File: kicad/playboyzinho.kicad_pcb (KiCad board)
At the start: 2 copper layers, 143.2 x 185.5 mm, 16 parts, among them SW1 SW_Push, SW2 SW_Push, SW3 SW_Push, SW4 SW_Push, SW5 SW_Push, SW6 SW_Push, SW7 SW_Push, SW8 SW_Push, SW9 SW_SPDT, U1 esp32-s3-pl, U7 (amplificador)_MAX98357_Module

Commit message: fix: corrige 90 graus
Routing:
- net /Button-2: track 93.2 -> 79.3 mm
- net /Button-3: track 106.6 -> 93.1 mm
- net /Button-4: track 86.4 -> 81.2 mm
- net /Button-1: track 88.0 -> 84.5 mm
- net /Button-5: track 52.0 -> 49.0 mm
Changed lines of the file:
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@@
+	)
+	(segment
+		(start 9.9385 84.4)
+		(end 18.0385 92.5)
+		(width 0.3)
+		(layer "F.Cu")
+		(net "/Button-4")
+	)
+	(segment
+		(start 21.87 94.5)
+		(end 21.87 123)
+		(width 0.3)
+		(layer "F.Cu")
+		(net "/Button-4")
 	)
 	(segment
@@
 	)
 	(segment
-		(start 28.87 92.5)
-		(end 28.87 130)
-		(width 0.3)
-		(layer "F.Cu")
-		(net "/Button-4")
-	)
-	(segment
-		(start 9.9385 84.4)
-		(end 18.0385 92.5)
-		(width 0.3)
-		(layer "F.Cu")
-		(net "/Button-4")
-	)
-	(segment
-		(start 28.87 130)
+		(start 18.0385 92.5)
+		(end 19.87 92.5)
+		(width 0.3)
+		(layer "F.Cu")
+		(net "/Button-4")
+	)
+	(segment
+		(start 21.87 123)
 		(end 38.87 140)
 		(width 0.3)
@@
 	)
 	(segment
-		(start 18.0385 92.5)
-		(end 28.87 92.5)
+		(start 19.87 92.5)
+		(end 21.87 94.5)
 		(width 0.3)
 		(layer "F.Cu")
@@
 	)
 	(segment
-		(start 77.37 93.05)
+		(start 71.32 87)
 		(end 85.25 100.93)
 		(width 0.3)
@@
 	(segment
 		(start 22.6985 87)
-		(end 77.37 87)
+		(end 71.32 87)
 		(width 0.3)
 		(layer "F.Cu")
@@
 	)
 	(segment
-		(start 77.37 87)
-		(end 77.37 93.05)
-		(width 0.3)
-		(layer "F.Cu")
-		(net "/Button-1")
-	)
-	(segment
 		(start 20.0985 84.4)
 		(end 22.6985 87)
@@
 	)
 	(segment
-		(start 21.6585 88.5)
-		(end 68.87 88.5)
-		(width 0.3)
-		(layer "F.Cu")
-		(net "/Button-2")
-	)
-	(segment
 		(start 17.5585 84.4)
 		(end 21.6585 88.5)
@@
 	)
 	(segment
-		(start 68.87 88.5)
-		(end 68.87 112.22)
+		(start 21.6585 88.5)
+		(end 45.15 88.5)
 		(width 0.3)
 		(layer "F.Cu")
@@
 	)
 	(segment
-		(start 68.87 112.22)
+		(start 45.15 88.5)
 		(end 71.65 115)
 		(width 0.3)
@@
 	)
 	(segment
-		(start 56.37 139)
+		(start 57.37 114)
 		(end 57.37 140)
+		(width 0.3)
+		(layer "F.Cu")
+		(net "/Button-3")
+	)
+	(segment
+		(start 20.6185 90)
+		(end 33.37 90)
 		(width 0.3)
 		(layer "F.Cu")
@@
 	)
 	(segment
-		(start 56.37 90)
-		(end 56.37 139)
-		(width 0.3)
-		(layer "F.Cu")
-		(net "/Button-3")
-	)
-	(segment
-		(start 20.6185 90)
-		(end 56.37 90)
+		(start 33.37 90)
+		(end 57.37 114)
 		(width 0.3)
 		(layer "F.Cu")
@@
 	)
 	(segment
-		(start 31.87 91.5)
-		(end 32.7 92.33)
+		(start 32.7 97.33)
+		(end 32.7 108.3)
 		(width 0.3)
 		(layer "F.Cu")
@@
 	)
 	(segment
-		(start 32.7 92.33)
-		(end 32.7 108.3)
+		(start 32.7 108.3)
+		(end 32.7 120.8)
+		(width 0.3)
+		(layer "F.Cu")
+		(net "/Button-5")
+	)
+	(segment
+		(start 19.5785 91.5)
+		(end 26.87 91.5)
 		(width 0.3)
 		(layer "F.Cu")
@@
 	)
 	(segment
-		(start 19.5785 91.5)
-		(end 31.87 91.5)
-		(width 0.3)
-		(layer "F.Cu")
-		(net "/Button-5")
-	)
-	(segment
-		(start 32.7 108.3)
-		(end 32.7 120.8)
-		(width 0.3)
-		(layer "F.Cu")
+		(start 26.87 91.5)
+		(end 32.7 97.33)
+		(width 0.3)
+		(layer "F.Cu")

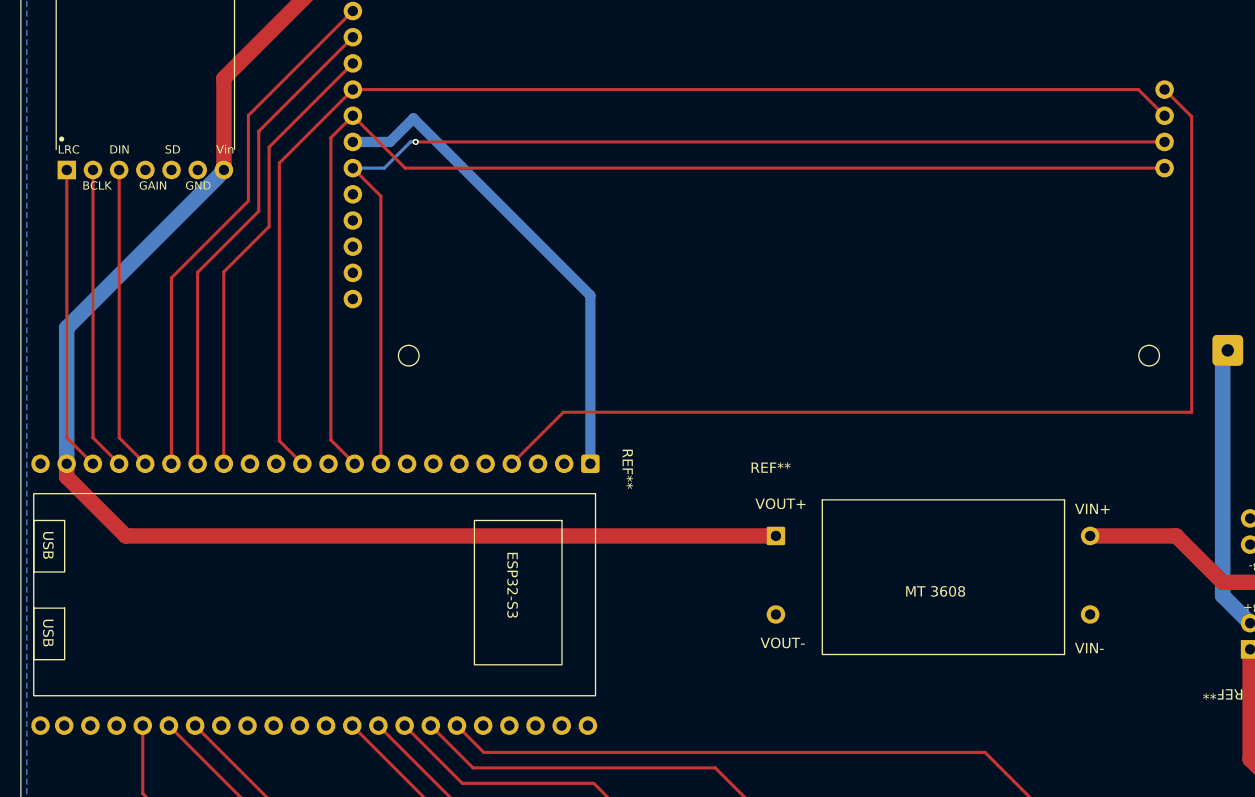
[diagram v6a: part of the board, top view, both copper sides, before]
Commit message: refact: separa conexões SD da tela e adiciona uma conexão ao SD do amplificador
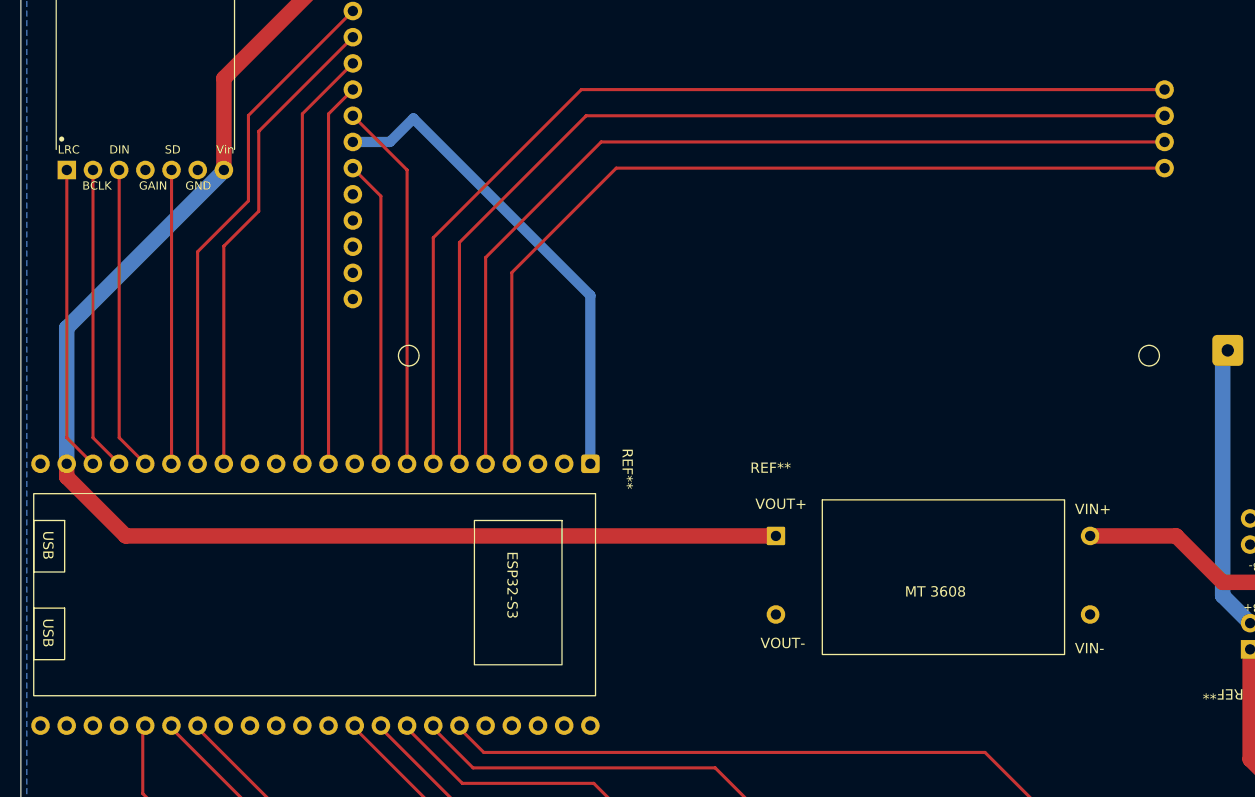
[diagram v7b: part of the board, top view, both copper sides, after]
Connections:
- U1 pad 10: /SCK -> unconnected-(U1-GPIO17-Pad10)
- U1 pad 11: unconnected-(U1-GPIO18-Pad11) -> /TFT_MOSI
- U1 pad 12: /MOSI -> /TFT_DC
- U1 pad 15: /DC -> /TFT_RESET
- U1 pad 16: /RESET -> /TFT_CS
- U1 pad 17: /CS -> /AMP_SD
- U1 pad 4: /SD_CS -> /SD_SCK
- U1 pad 5: unconnected-(U1-GPIO5-Pad5) -> /SD_MISO
- U1 pad 6: unconnected-(U1-GPIO6-Pad6) -> /SD_MOSI
- U1 pad 7: unconnected-(U1-GPIO7-Pad7) -> /SD_CS
- U1 pad 8: unconnected-(U1-GPIO15-Pad8) -> /TFT_SCK
- U1 pad 9: /MISO -> /TFT_MISO
- U4 pad 16: /MOSI -> /SD_MOSI
- U4 pad 17: /MISO -> /SD_MISO
- U4 pad 18: /SCK -> /SD_SCK
- U4 pad 3: /CS -> /TFT_CS
- U4 pad 4: /RESET -> /TFT_RESET
- U4 pad 5: /DC -> /TFT_DC
- U4 pad 6: /MOSI -> /TFT_MOSI
- U4 pad 7: /SCK -> /TFT_SCK
- U4 pad 9: /MISO -> /TFT_MISO
- U7 pad 5: unconnected-(U7-SD-Pad5) -> /AMP_SD
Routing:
- net /MOSI: track 120.0 -> 0.00 mm
- net /SCK: track 116.4 -> 0.00 mm
- net /MISO: track 109.6 -> 0.00 mm, vias 1 -> 0
- net /SD_MOSI: track 0.00 -> 95.0 mm
- net /SD_MISO: track 0.00 -> 90.5 mm
- net /SD_SCK: track 0.00 -> 86.1 mm
- net /CS: track 51.2 -> 0.00 mm
- net /TFT_CS: track 0.00 -> 50.2 mm
- net /RESET: track 47.6 -> 0.00 mm
- net /TFT_RESET: track 0.00 -> 46.6 mm
- net /DC: track 44.0 -> 0.00 mm
- net /TFT_DC: track 0.00 -> 40.9 mm
- net /TFT_MOSI: track 0.00 -> 37.3 mm
- net /TFT_SCK: track 0.00 -> 35.9 mm
- net /TFT_MISO: track 0.00 -> 29.8 mm
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
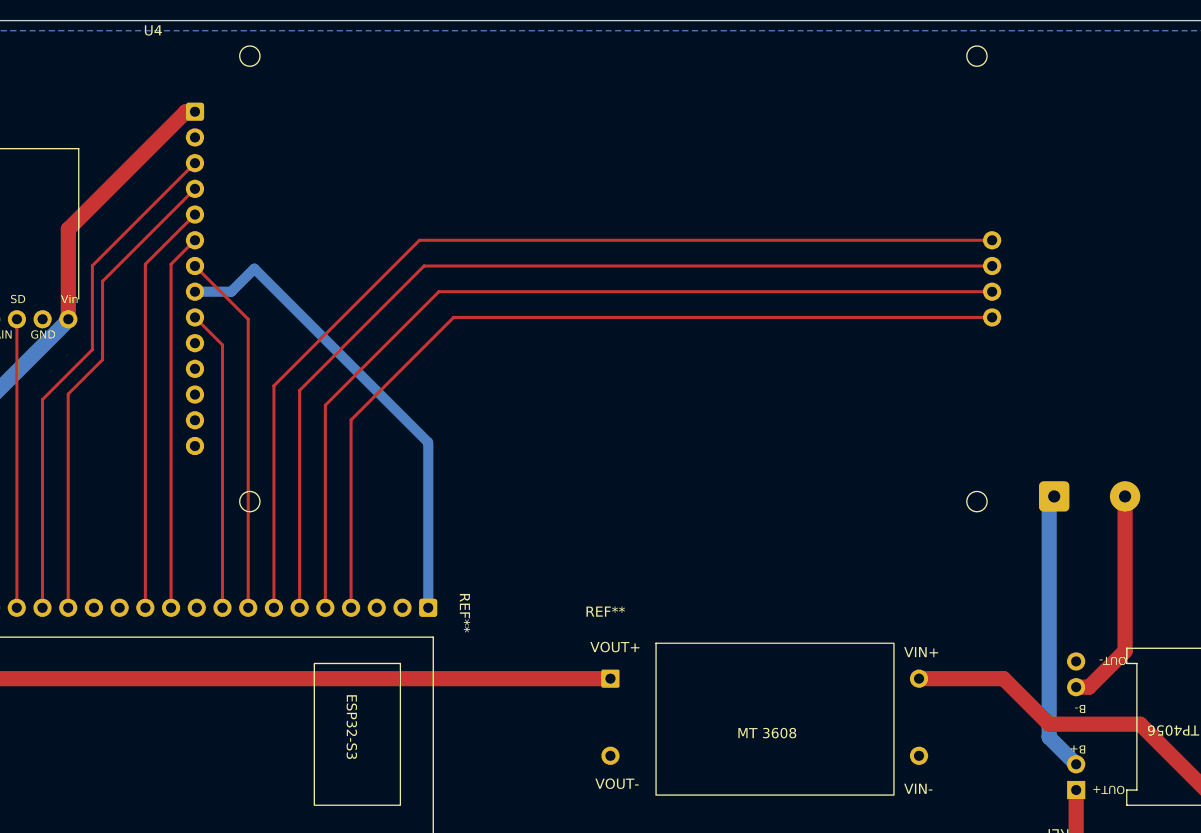
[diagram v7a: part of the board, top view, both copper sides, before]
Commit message: refact: muda código para condizer com esquemático (novos pinos para conectar sd e tela separados) e corrige tamanho da tela
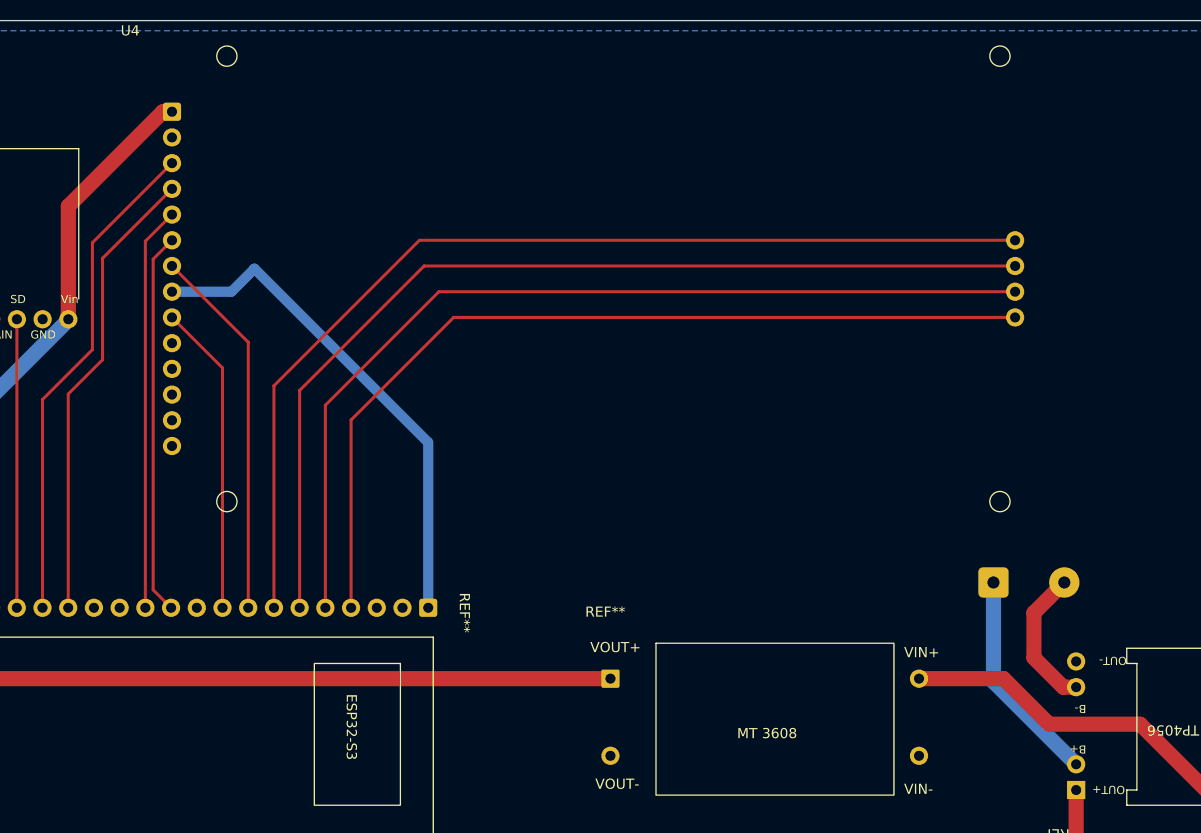
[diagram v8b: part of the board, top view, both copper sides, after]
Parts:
- moved U2 10.4 mm to (88.9, 56.5)
- moved U4 2.27 mm to (7.73, 10.0)
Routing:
- net -BATT: track 21.6 -> 14.1 mm
- net +BATT: track 27.8 -> 21.3 mm
- net /SD_SCK: track 86.1 -> 88.3 mm
- net /SD_MOSI: track 95.0 -> 97.2 mm
- net /SD_MISO: track 90.5 -> 92.8 mm
- net /3V3: track 47.4 -> 49.7 mm
- net /SD_CS: track 98.8 -> 101.1 mm
- net +5V: track 133.5 -> 132.5 mm
- net /TFT_SCK: track 35.9 -> 36.9 mm
- net /TFT_DC: track 40.9 -> 39.9 mm
- net /TFT_RESET: track 46.6 -> 45.6 mm
- net /TFT_MISO: track 29.8 -> 30.7 mm
- net /TFT_CS: track 50.2 -> 49.2 mm
- net /TFT_MOSI: track 37.3 -> 37.8 mm
